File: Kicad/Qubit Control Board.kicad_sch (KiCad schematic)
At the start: 144 parts, among them J1 USB_C_Receptacle_PowerOnly_6P, J2 CLK_Pins, J3 Idata, J4 Qdata, J5 SPIdata, J6 SMA, U1 LT3045xMSE, U2 TRF372017IRGZR, U3 LT3045xMSE, U4 LT3045xMSE, U5 SN65LVDS1DBV, U6 AD9743BCPZ, Y2 CVHD-950-100.000

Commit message: Finshed 1.8/3.3V LDO redo
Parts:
- CIN2: footprint Capacitor_SMD:C_0402_1005Metric -> Capacitor_SMD:C_0603_1608Metric
- CLDO1, CLDO2: footprint Capacitor_SMD:C_1206_3216Metric_Pad1.33x1.80mm_HandSolder -> Capacitor_SMD:C_0603_1608Metric
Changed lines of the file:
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@@
 			)
 		)
-		(property "Footprint" "Capacitor_SMD:C_1206_3216Metric_Pad1.33x1.80mm_HandSolder"
+		(property "Footprint" "Capacitor_SMD:C_0603_1608Metric"
 			(at 129.2352 54.61 0)
 			(hide yes)
@@
 			)
 		)
-		(property "Footprint" "Capacitor_SMD:C_0402_1005Metric"
+		(property "Footprint" "Capacitor_SMD:C_0603_1608Metric"
 			(at 106.3752 71.12 0)
 			(hide yes)
@@
 			)
 		)
-		(property "Footprint" "Capacitor_SMD:C_1206_3216Metric_Pad1.33x1.80mm_HandSolder"
+		(property "Footprint" "Capacitor_SMD:C_0603_1608Metric"
 			(at 143.2052 54.61 0)
 			(hide yes)

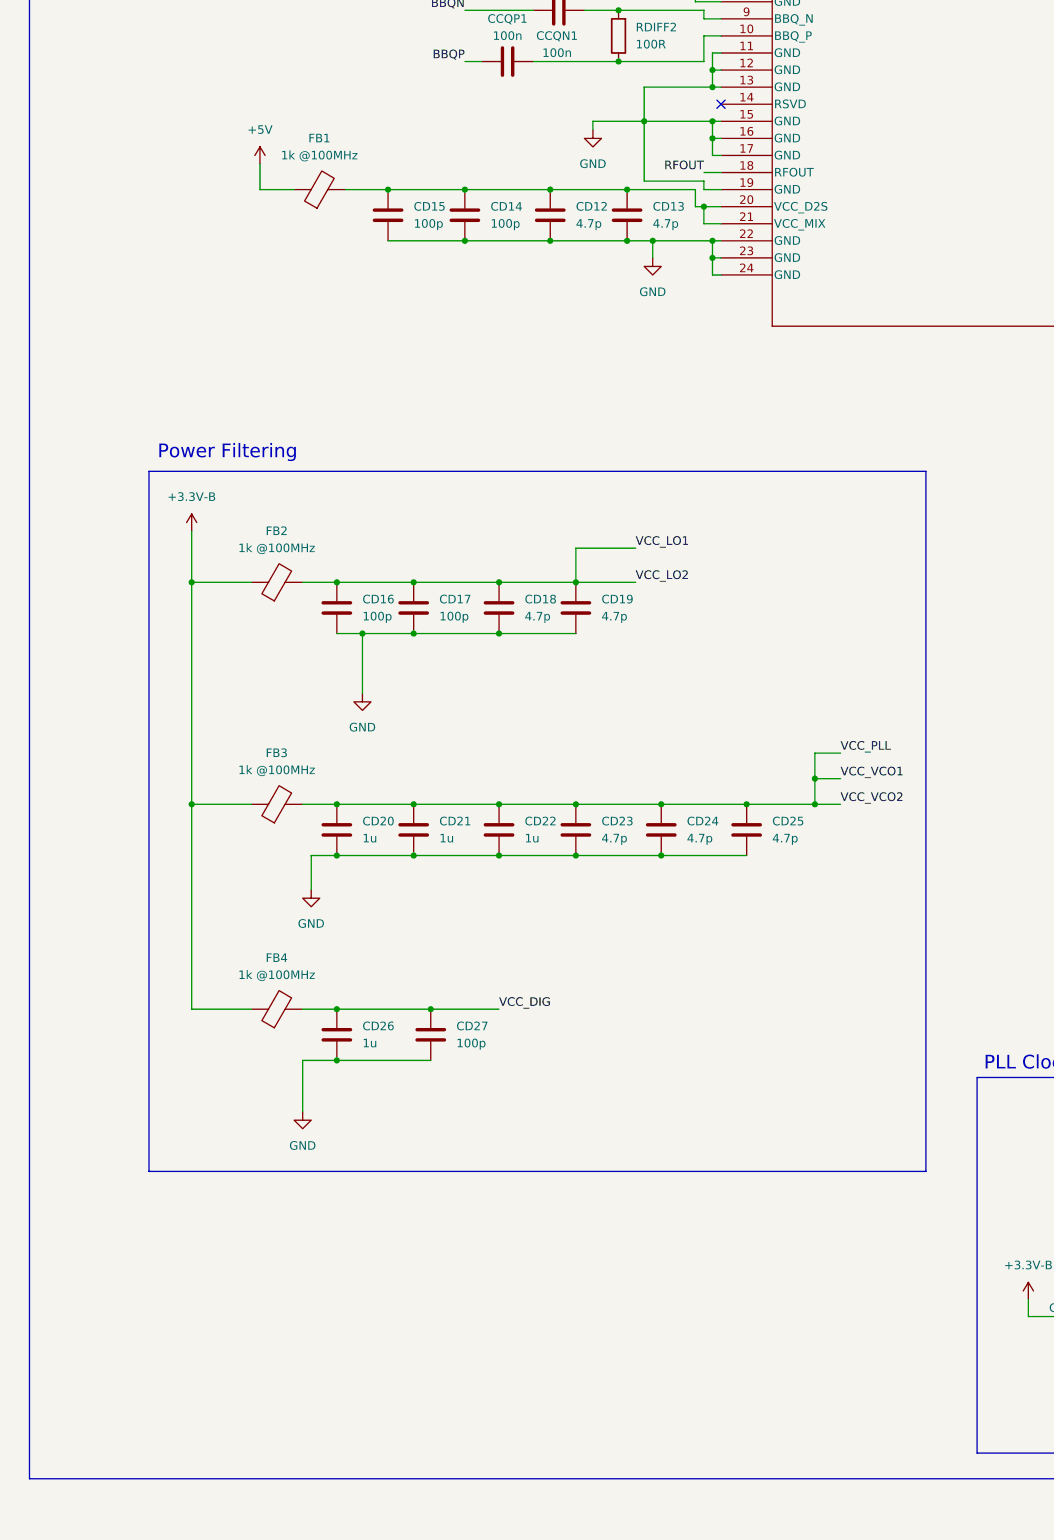
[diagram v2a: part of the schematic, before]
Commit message: added extra F beads to PLL power input
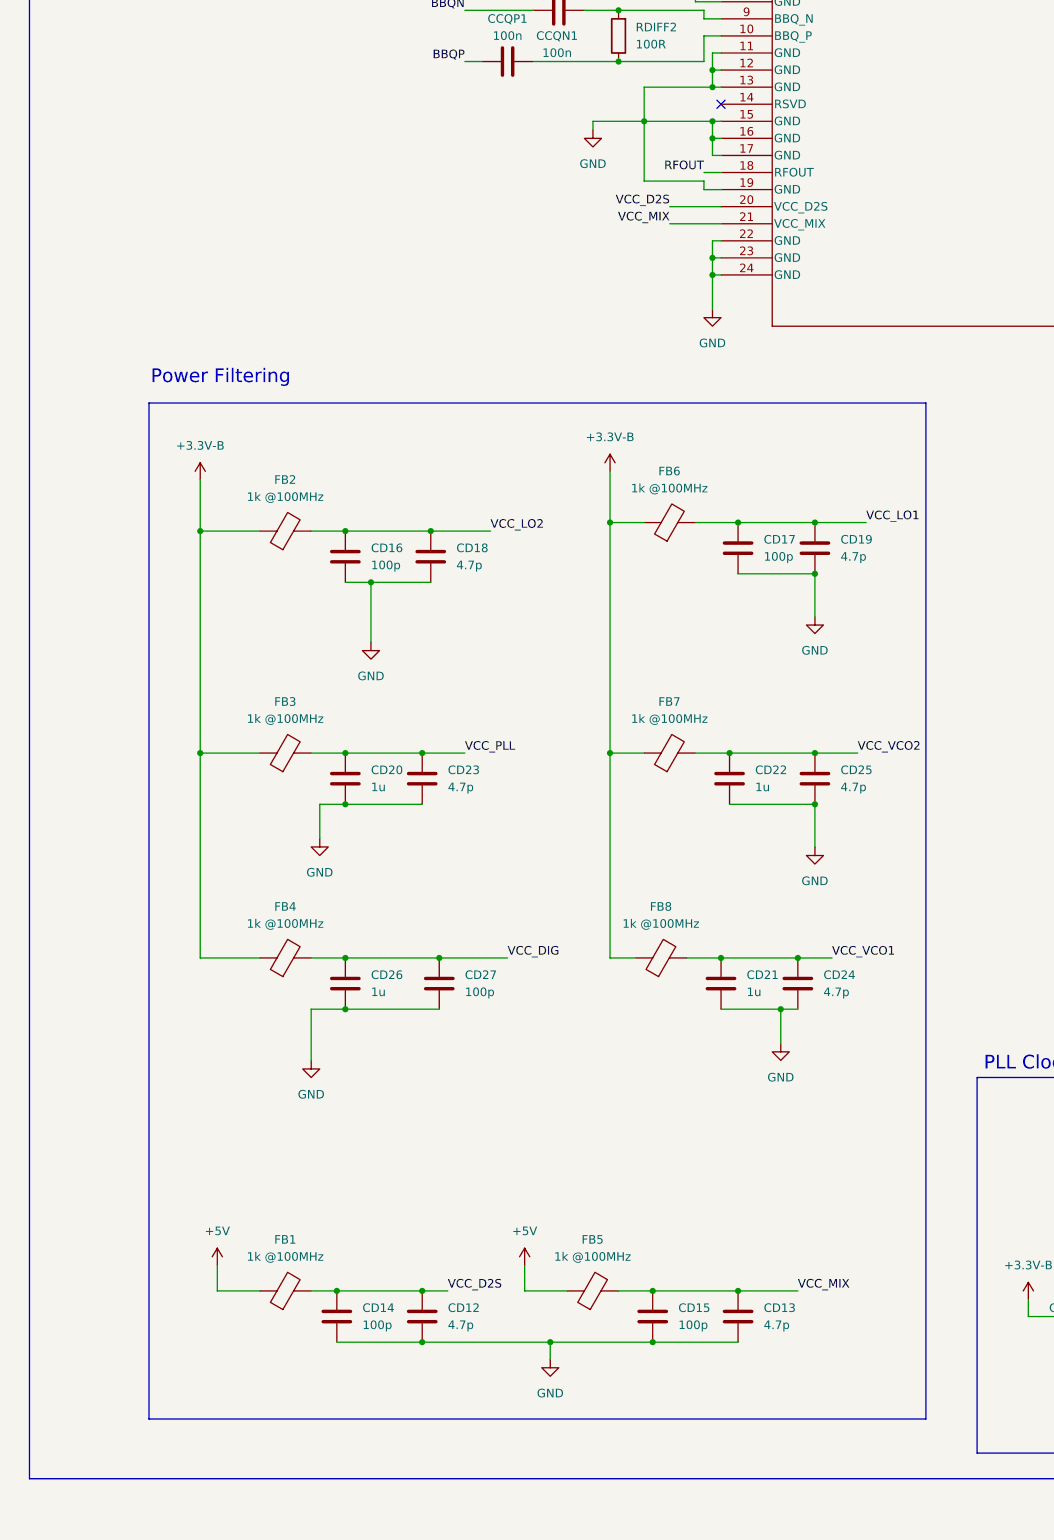
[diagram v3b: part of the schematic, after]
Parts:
- added FB5, FB6, FB7, FB8: 1k @100MHz, Inductor_SMD:L_0603_1608Metric_Pad1.05x0.95mm_HandSolder, symbol Device:FerriteBead
- RDIFF2, RDIFF3: footprint Resistor_SMD:R_0603_1608Metric -> Resistor_SMD:R_0402_1005Metric
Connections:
- net +3.3V-B: now also FB6.1, FB7.1, FB8.1
- net +5V: now also FB5.1
- net VCC_LO1: now also FB6.2; no longer CD16.2, CD18.2, FB2.2, U2.30 (VCC_LO2)
- net VCC_PLL: no longer CD21.2, CD22.2, CD24.2, CD25.2, U2.32 (VCC_VCO2), U2.35 (VCC_VCO1)
- net VCC_D2S: now reaches CD12.2, CD14.2, FB1.2, U2.20 (VCC_D2S)
- net VCC_D2S: no longer CD13.2, CD15.2, U2.21 (VCC_MIX)
- new net VCC_LO2: CD16.2, CD18.2, FB2.2, U2.30 (VCC_LO2)
- new net VCC_MIX: CD13.2, CD15.2, FB5.2, U2.21 (VCC_MIX)
- new net VCC_VCO1: CD21.2, CD24.2, FB8.2, U2.35 (VCC_VCO1)
- new net VCC_VCO2: CD22.2, CD25.2, FB7.2, U2.32 (VCC_VCO2)
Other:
- moved on the sheet: CD12, CD13, CD14, CD15, CD16, CD17, CD18, CD19, CD20, CD21, CD22, CD23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

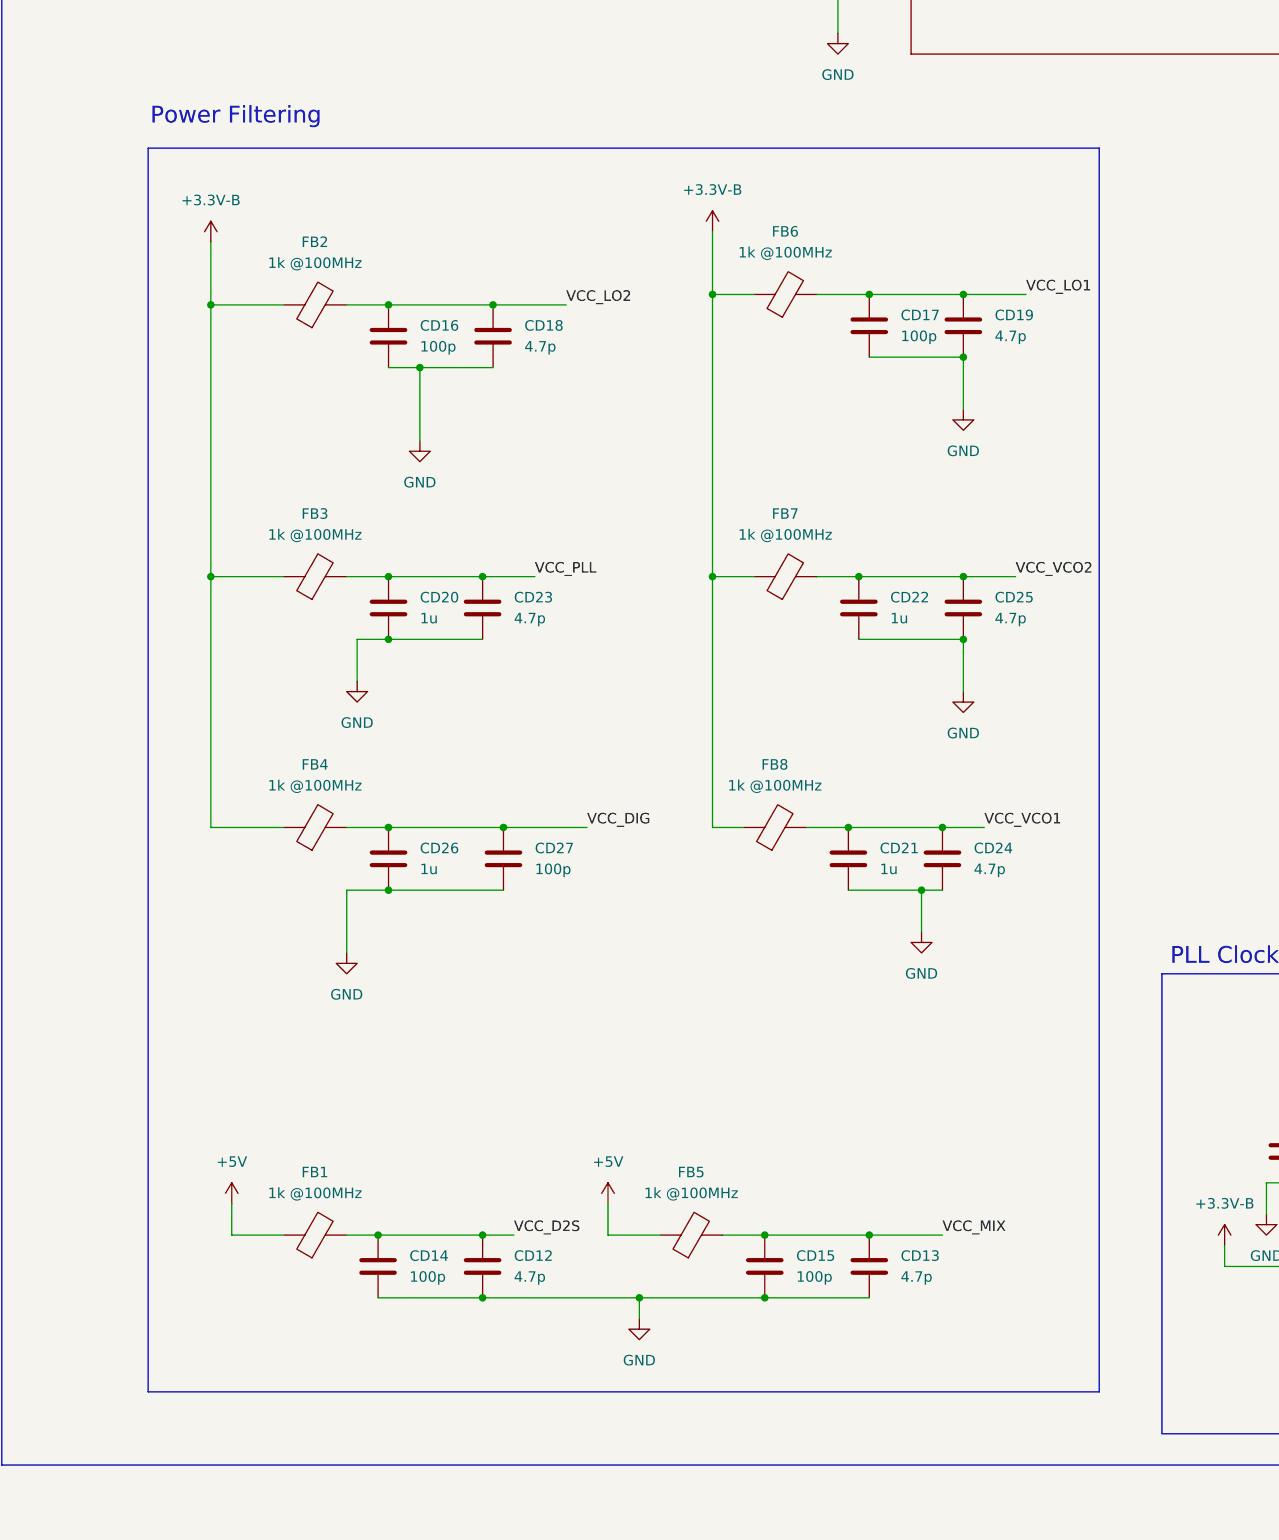
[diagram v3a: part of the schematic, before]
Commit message: LF edits and cap resizing
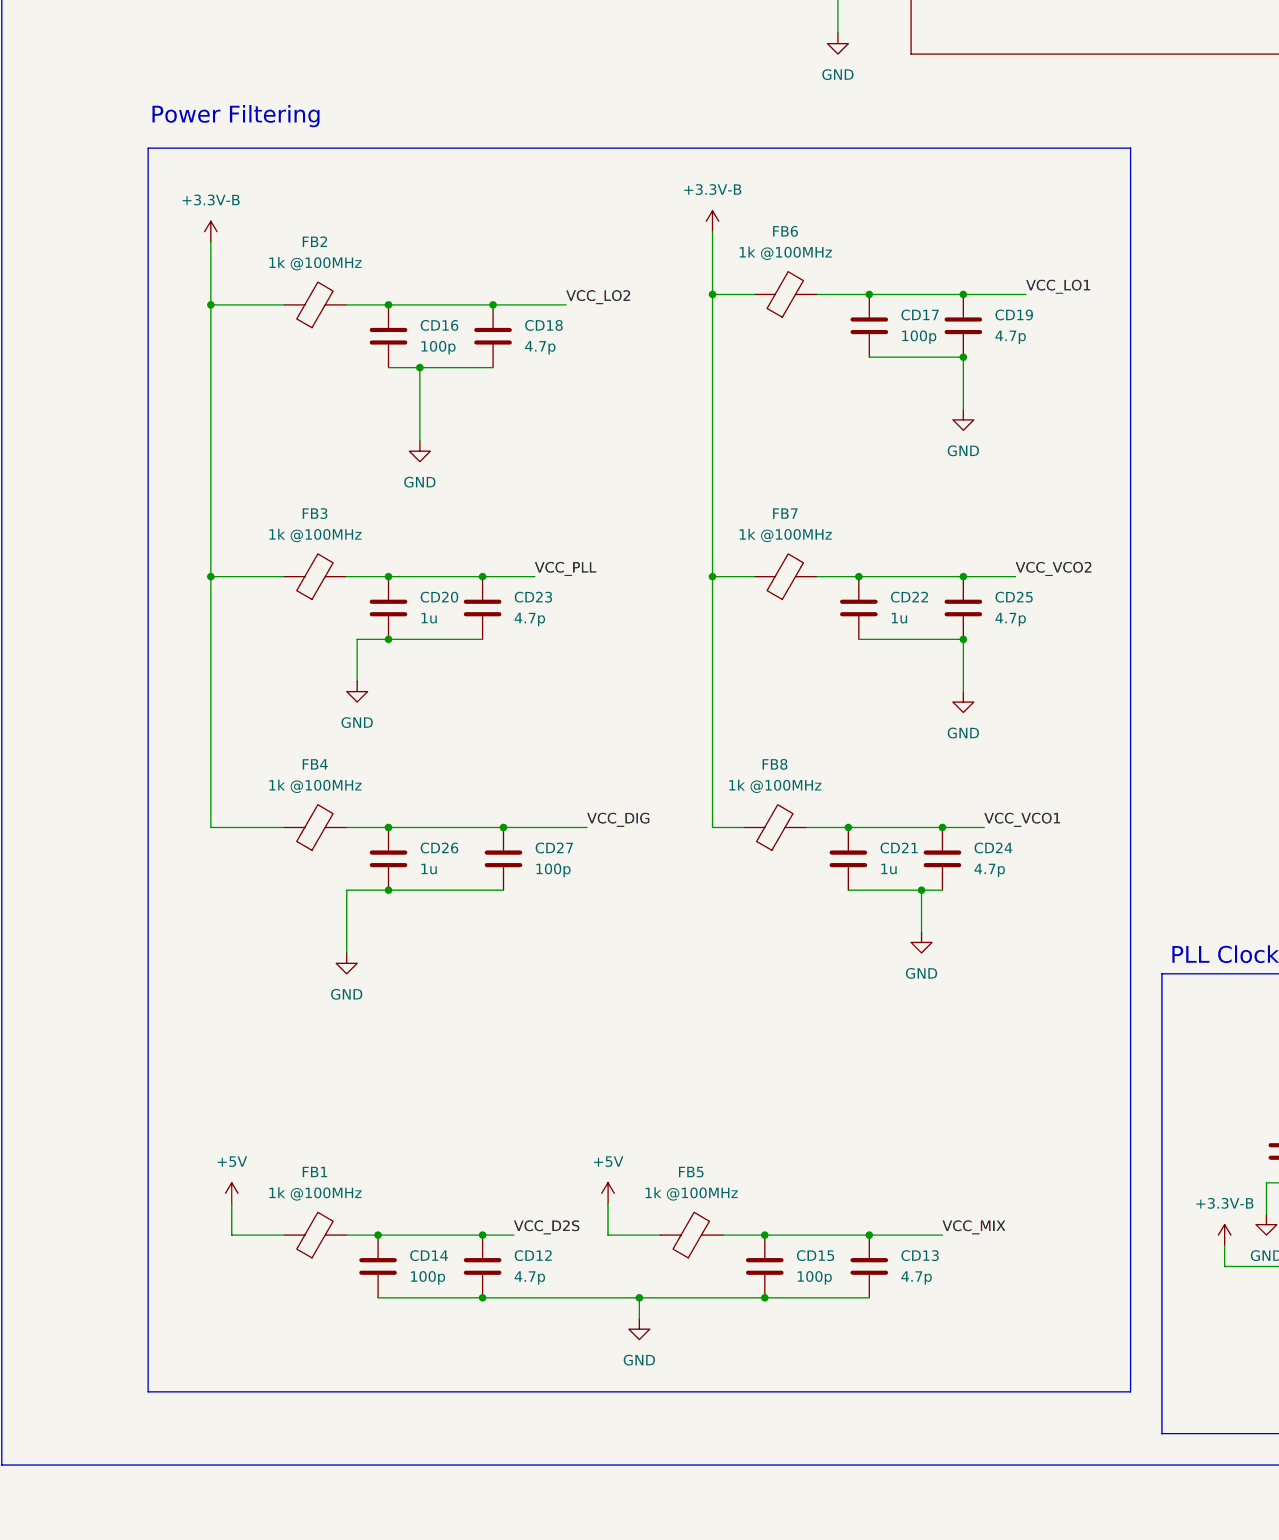
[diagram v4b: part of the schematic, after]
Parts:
- CD2, CD3: footprint Capacitor_SMD:C_0201_0603Metric -> Capacitor_SMD:C_0402_1005Metric
- CLF1, CLF2, CLF3: footprint Capacitor_SMD:C_0603_1608Metric -> Capacitor_SMD:C_0402_1005Metric
- RLF1, RLF2: footprint Resistor_SMD:R_0603_1608Metric -> Resistor_SMD:R_0402_1005Metric
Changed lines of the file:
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@@
 	(rectangle
 		(start 346.71 204.47)
-		(end 462.28 355.6)
+		(end 466.09 355.6)
 		(stroke
 			(width 0)
@@
 			)
 		)
-		(property "Footprint" "Capacitor_SMD:C_0603_1608Metric"
+		(property "Footprint" "Capacitor_SMD:C_0402_1005Metric"
 			(at 373.0752 110.49 0)
 			(hide yes)
@@
 			)
 		)
-		(property "Footprint" "Resistor_SMD:R_0603_1608Metric"
+		(property "Footprint" "Resistor_SMD:R_0402_1005Metric"
 			(at 370.332 116.84 90)
 			(hide yes)
@@
 			)
 		)
-		(property "Footprint" "Capacitor_SMD:C_0603_1608Metric"
+		(property "Footprint" "Capacitor_SMD:C_0402_1005Metric"
 			(at 360.3752 110.49 0)
 			(hide yes)
@@
 			)
 		)
-		(property "Footprint" "Resistor_SMD:R_0603_1608Metric"
+		(property "Footprint" "Resistor_SMD:R_0402_1005Metric"
 			(at 383.54 104.648 90)
 			(hide yes)
@@
 			)
 		)
-		(property "Footprint" "Capacitor_SMD:C_0603_1608Metric"
+		(property "Footprint" "Capacitor_SMD:C_0402_1005Metric"
 			(at 393.3952 110.49 0)
 			(hide yes)
@@
 			)
 		)
-		(property "Footprint" "Capacitor_SMD:C_0201_0603Metric"
+		(property "Footprint" "Capacitor_SMD:C_0402_1005Metric"
 			(at 151.4348 198.12 0)
 			(hide yes)
@@
 			)
 		)
-		(property "Footprint" "Capacitor_SMD:C_0201_0603Metric"
+		(property "Footprint" "Capacitor_SMD:C_0402_1005Metric"
 			(at 162.8648 198.12 0)
 			(hide yes)
